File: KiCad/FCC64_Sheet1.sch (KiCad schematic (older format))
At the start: 23 parts, among them P1 JTAG, U1 27C256, U2 ATF1504AS, Y1 C64-Expansionport

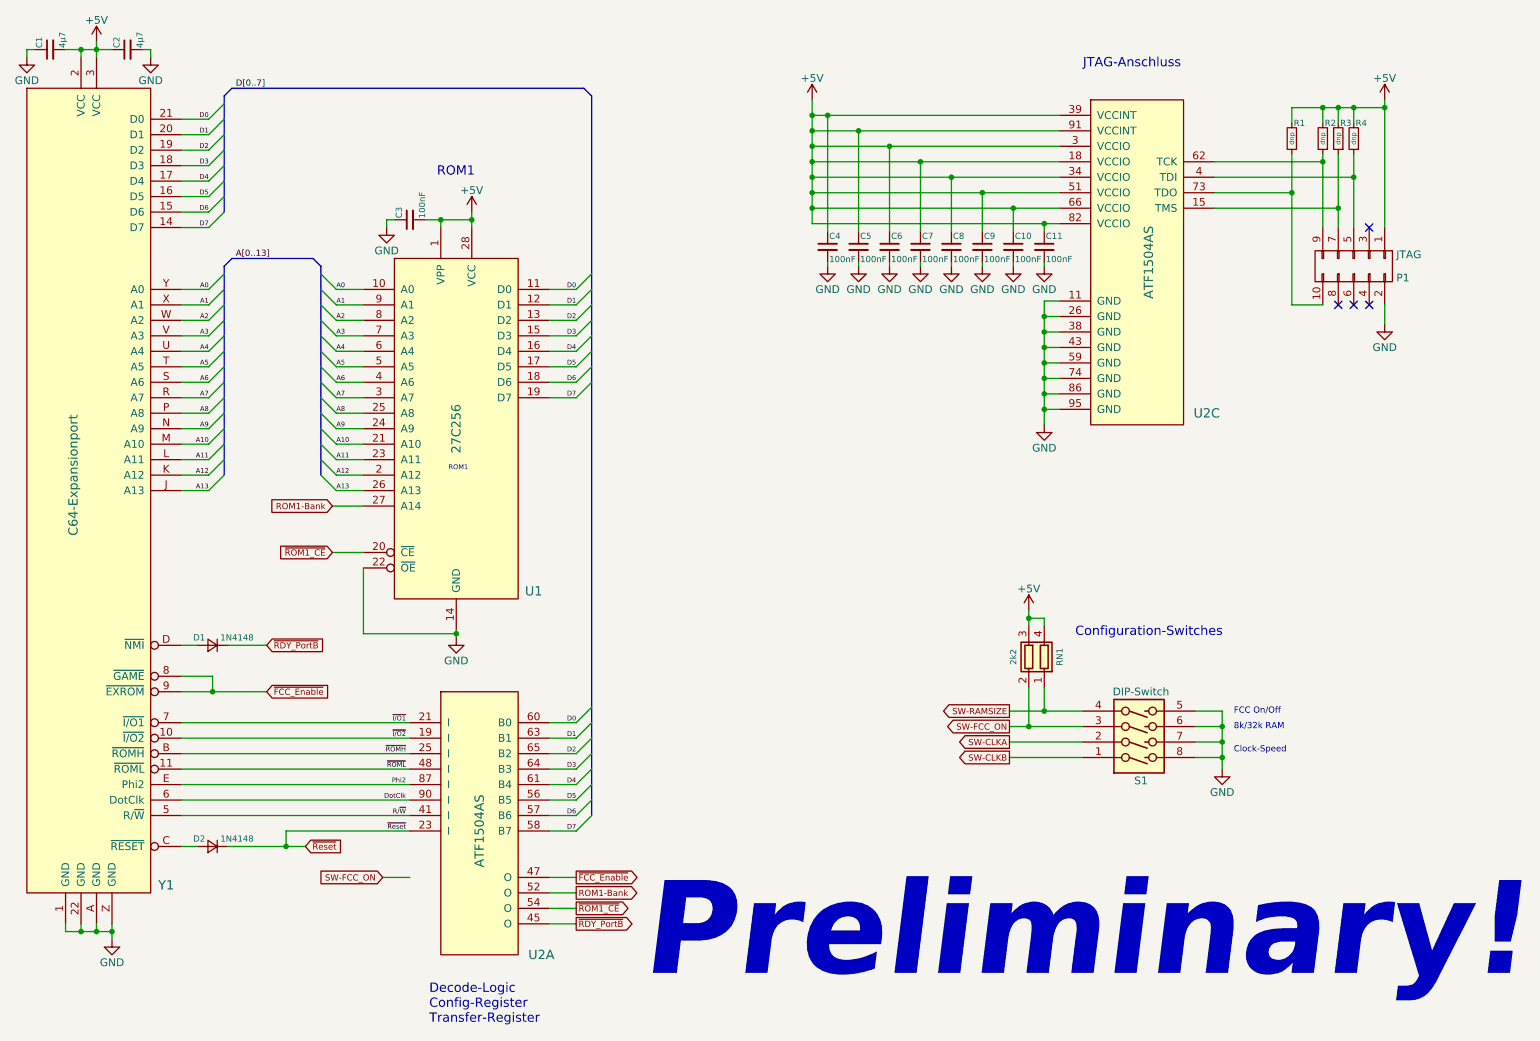
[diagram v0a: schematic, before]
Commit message: Various issues solved:
* QFP44-Footprint for W65C02 corrected
* FCC-On/Off deleted
* new battery supervisor ic TPS6513-01
* Battery Holder corrected
* Signals D5 and D7 to CPLD swapped
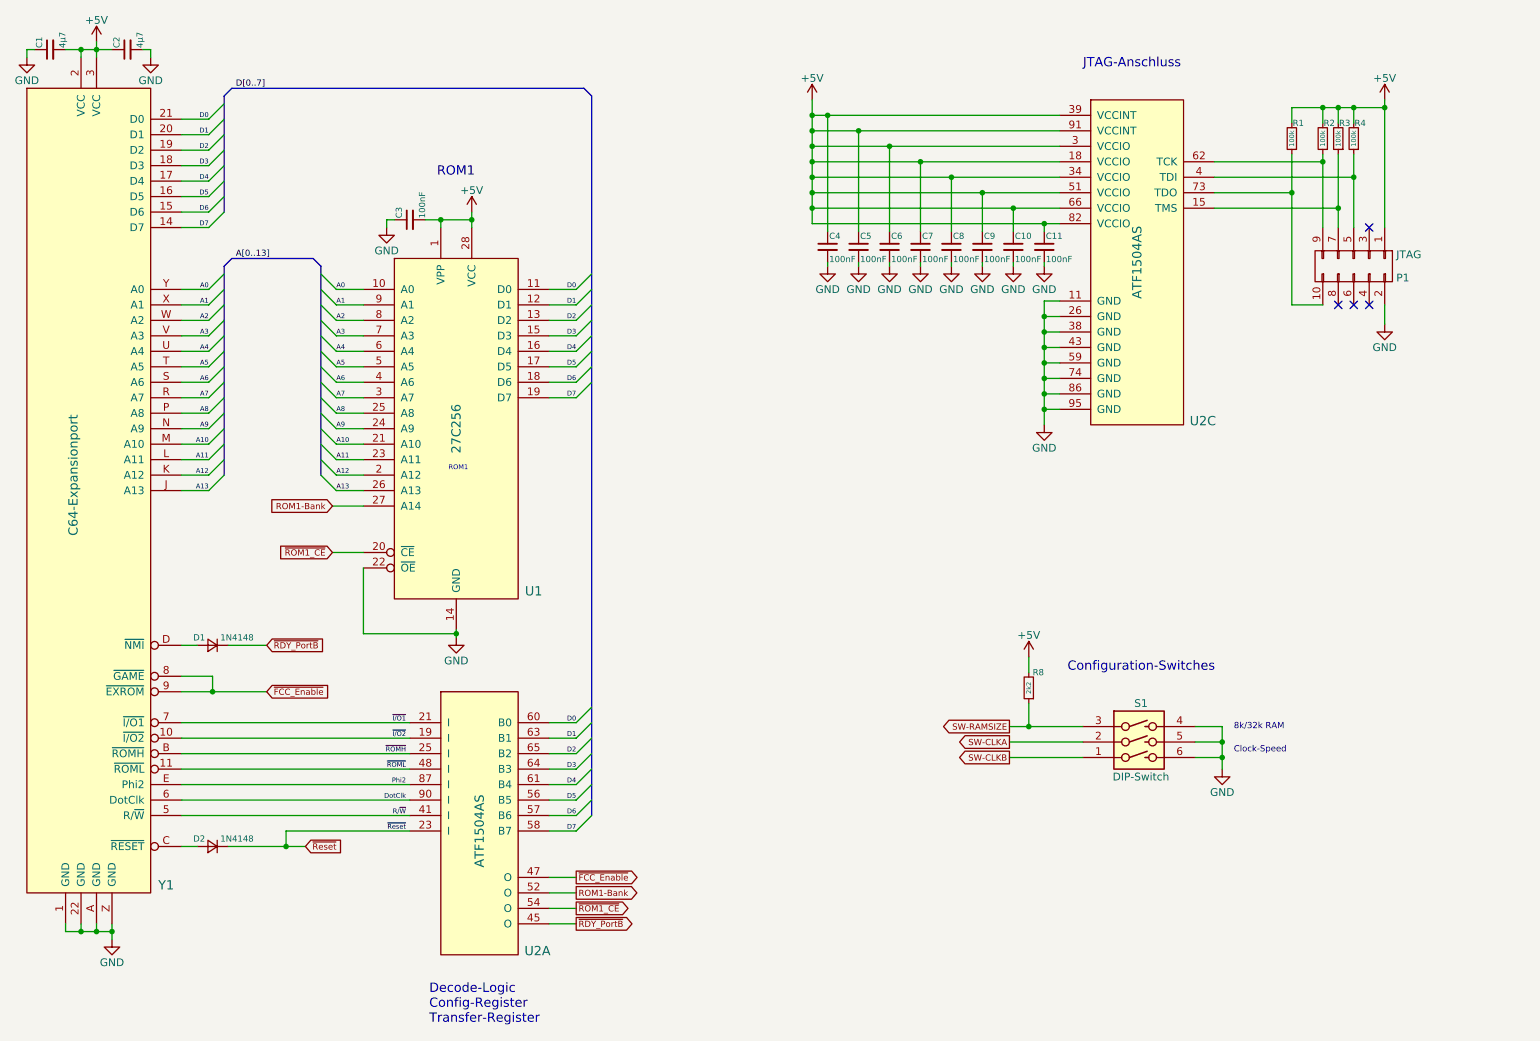
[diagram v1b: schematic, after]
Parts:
- removed RN1: 2k2, TTB_MyLib:TTB_RNet1206_2R, symbol R_Pack02
- removed S1: DIP-Switch, TTB_MyLib:TTB_DIPSwitch4, symbol DIP-Switch_4fach
- added R8: 2k2, TTB_MyLib:TTB_R0603, symbol R_Small
- added S1: DIP-Switch, TTB_MyLib:TTB_DIPSwitch3, symbol DIP-Switch_3fach
- R1, R2, R3, R4: value dnp -> 100k
- U2: footprint Housings_QFP:TQFP-100_14x14mm_Pitch0.5mm -> TTB_MyLib:TTB_TQFP100
- U2: footprint (none) -> TTB_MyLib:TTB_TQFP100
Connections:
- net +5V: now also R8.2
- net GND: now also S1.4 (P4), S1.5 (P5), S1.6 (P6)
- net SW-CLKA: now also S1.2 (P2)
- net SW-CLKB: now also S1.1 (P1)
- net SW-RAMSIZE: now also R8.1, S1.3 (P3)
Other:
- note removed: "FCC On/Off"
- note removed: "Preliminary!"
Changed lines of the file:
@@
 Sheet 2 3
 Title "The Final Chesscard (Forum64-Edition 2017)"
-Date "2017-05-04"
-Rev "-"
+Date "2017-07-09"
+Rev "1.0"
 Comp ""
 Comment1 ""
@@
 R/~W
 $Comp
-L ATF1504-RESCUE-FCC64 U?
-U 3 1 58FE4728
-P 8700 2475
-AR Path="/58FE4728" Ref="U?"  Part="3"
-AR Path="/58E6A155/58FE4728" Ref="U2"  Part="3"
-F 0 "U2" H 9150 1500 60  0000 C CNN
-F 1 "ATF1504AS" V 8775 2475 60  0000 C CNN
-F 2 "Housings_QFP:TQFP-100_14x14mm_Pitch0.5mm" H 8700 2275 60  0001 C CNN
-F 3 "" H 8700 2275 60  0000 C CNN
-	3    8700 2475
-	1    0    0    -1
-$EndComp
-$Comp
 L CONN_02X05 P1
 U 1 1 58FE4D90
@@
 U 1 1 58FE6795
 P 9900 1675
-F 0 "R2" H 9815 1575 40  0000 L CNN
-F 1 "dnp" V 9900 1675 31  0000 C CNN
+F 0 "R2" H 9895 1575 40  0000 R CNN
+F 1 "100k" V 9900 1675 31  0000 C CNN
 F 2 "TTB_MyLib:TTB_R0603" H 9900 1675 50  0001 C CNN
 F 3 "" H 9900 1675 50  0000 C CNN
@@
 U 1 1 58FE69EA
 P 10000 1675
-F 0 "R3" H 9915 1575 40  0000 L CNN
-F 1 "dnp" V 10000 1675 31  0000 C CNN
+F 0 "R3" H 9995 1575 40  0000 R CNN
+F 1 "100k" V 10000 1675 31  0000 C CNN
 F 2 "TTB_MyLib:TTB_R0603" H 10000 1675 50  0001 C CNN
 F 3 "" H 10000 1675 50  0000 C CNN
@@
 U 1 1 58FE6A19
 P 10100 1675
-F 0 "R4" H 10015 1575 40  0000 L CNN
-F 1 "dnp" V 10100 1675 31  0000 C CNN
+F 0 "R4" H 10095 1575 40  0000 R CNN
+F 1 "100k" V 10100 1675 31  0000 C CNN
 F 2 "TTB_MyLib:TTB_R0603" H 10100 1675 50  0001 C CNN
 F 3 "" H 10100 1675 50  0000 C CNN
@@
 U 1 1 58FE6F40
 P 9700 1675
-F 0 "R1" H 9615 1575 40  0000 L CNN
-F 1 "dnp" V 9700 1675 31  0000 C CNN
+F 0 "R1" H 9695 1575 40  0000 R CNN
+F 1 "100k" V 9700 1675 31  0000 C CNN
 F 2 "TTB_MyLib:TTB_R0603" H 9700 1675 50  0001 C CNN
 F 3 "" H 9700 1675 50  0000 C CNN
@@
 	1525 1100 1525 1150
 Connection ~ 1875 1100
-Text GLabel 3825 6450 0    40   Input ~ 0
-SW-FCC_ON
-Wire Wire Line
-	3825 6450 4000 6450
-Text Notes 8300 4900 0    60   ~ 0
+Text Notes 8250 5125 0    60   ~ 0
 Configuration-Switches
-Text GLabel 7875 5375 0    40   Output ~ 0
+Text GLabel 7875 5475 0    40   Output ~ 0
 SW-RAMSIZE
 Text GLabel 7875 5675 0    40   Output ~ 0
@@
 L +5V #PWR020
 U 1 1 590A9614
-P 8000 4725
-F 0 "#PWR020" H 8000 4575 50  0001 C CNN
-F 1 "+5V" H 8000 4865 50  0000 C CNN
-F 2 "" H 8000 4725 50  0000 C CNN
-F 3 "" H 8000 4725 50  0000 C CNN
-	1    8000 4725
-	1    0    0    -1
-$EndComp
-Wire Wire Line
-	7875 5375 8350 5375
+P 8000 5025
+F 0 "#PWR020" H 8000 4875 50  0001 C CNN
+F 1 "+5V" H 8000 5165 50  0000 C CNN
+F 2 "" H 8000 5025 50  0000 C CNN
+F 3 "" H 8000 5025 50  0000 C CNN
+	1    8000 5025
+	1    0    0    -1
+$EndComp
 Wire Wire Line
 	7875 5475 8350 5475
 Wire Wire Line
 	7875 5575 8350 5575
-Text GLabel 7875 5475 0    40   Output ~ 0
-SW-FCC_ON
 $Comp
 L GND #PWR021
@@
 	9250 5575 9075 5575
 Wire Wire Line
-	9250 5375 9250 5750
-Wire Wire Line
 	9075 5475 9250 5475
 Connection ~ 9250 5575
 Wire Wire Line
-	9075 5375 9250 5375
-Connection ~ 9250 5475
-$Comp
-L DIP-Switch_4fach S1
-U 1 1 590A9635
-P 8725 5525
-F 0 "S1" H 8725 5825 50  0000 C CNN
-F 1 "DIP-Switch" H 8725 5250 50  0000 C CNN
-F 2 "TTB_MyLib:TTB_DIPSwitch4" H 8700 5525 50  0001 C CNN
-F 3 "" H 8700 5525 50  0000 C CNN
-	1    8725 5525
-	1    0    0    1
-$EndComp
-Wire Wire Line
-	9075 5675 9250 5675
+	9250 5675 9075 5675
 Connection ~ 9250 5675
 Text Notes 9325 5500 0    40   ~ 0
 8k/32k RAM
-Text Notes 9325 5400 0    40   ~ 0
-FCC On/Off
 Text Notes 9325 5650 0    40   ~ 0
 Clock-Speed
-$Comp
-L R_Pack02 RN1
-U 1 1 590C2924
-P 8000 5025
-F 0 "RN1" V 7800 5025 40  0000 C CNN
-F 1 "2k2" V 8100 5025 40  0000 C CNN
-F 2 "TTB_MyLib:TTB_RNet1206_2R" V 8175 5025 50  0001 C CNN
-F 3 "" H 8000 5025 50  0000 C CNN
-	1    8000 5025
-	-1   0    0    -1
-$EndComp
 Wire Wire Line
 	7875 5675 8350 5675
 Wire Wire Line
-	8000 4825 8000 4725
-Wire Wire Line
-	8100 4825 8100 4775
-Wire Wire Line
-	8100 4775 8000 4775
-Connection ~ 8000 4775
-Text Notes 11225 7150 2    600  Italic 120
-Preliminary!
+	8000 5125 8000 5025
+Wire Wire Line
+	8000 5325 8000 5475
+Connection ~ 8000 5475
+$Comp
+L ATF1504-RESCUE-FCC64 U2
+U 3 1 595BDF95
+P 8700 2475
+AR Path="/595BDF95" Ref="U2"  Part="3"
+AR Path="/58E6A155/595BDF95" Ref="U2"  Part="3"
+F 0 "U2" H 9125 1450 60  0000 C CNN
+F 1 "ATF1504AS" V 8700 2475 60  0000 C CNN
+F 2 "TTB_MyLib:TTB_TQFP100" H 8700 2275 60  0001 C CNN
+F 3 "" H 8700 2275 60  0000 C CNN
+	3    8700 2475
+	1    0    0    -1
+$EndComp
+$Comp
+L DIP-Switch_3fach S1
+U 1 1 59624767
+P 8725 5575
+F 0 "S1" H 8725 5825 50  0000 C CNN
+F 1 "DIP-Switch" H 8725 5350 50  0000 C CNN
+F 2 "TTB_MyLib:TTB_DIPSwitch3" H 8700 5575 50  0001 C CNN
+F 3 "" H 8700 5575 50  0000 C CNN
+	1    8725 5575
+	1    0    0    -1
+$EndComp
+Wire Wire Line
+	9250 5475 9250 5750
+$Comp
+L R_Small R8
+U 1 1 59626FD6
+P 8000 5225
+F 0 "R8" H 7975 5125 40  0000 R CNN
+F 1 "2k2" V 8000 5225 31  0000 C CNN
+F 2 "TTB_MyLib:TTB_R0603" H 8000 5225 50  0001 C CNN
+F 3 "" H 8000 5225 50  0000 C CNN
+	1    8000 5225
+	-1   0    0    1
+$EndComp
 $Comp
 L ATF1504 U2
-U 1 1 59219D32
+U 1 1 59631F49
 P 4450 6150
-F 0 "U2" H 4850 5350 60  0000 C CNN
+F 0 "U2" H 4825 5375 60  0000 C CNN
 F 1 "ATF1504AS" V 4450 6150 60  0000 C CNN
-F 2 "" H 4450 5950 60  0000 C CNN
+F 2 "TTB_MyLib:TTB_TQFP100" H 4450 5950 60  0001 C CNN
 F 3 "" H 4450 5950 60  0000 C CNN
 	1    4450 6150
 	1    0    0    -1
 $EndComp
-Wire Wire Line
-	8000 5225 8000 5475
-Connection ~ 8000 5475
-Wire Wire Line
-	8100 5225 8100 5375
-Connection ~ 8100 5375
 $EndSCHEMATC

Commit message: Tidying up for initial batch
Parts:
- C1, C2: value 4µ7 -> 10µ
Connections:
- net GND: now also S1.1 (P1), S1.2 (P2), S1.3 (P3); no longer S1.4 (P4), S1.5 (P5), S1.6 (P6)
- net SW-CLKA: now also S1.5 (P5); no longer S1.2 (P2)
- net SW-CLKB: now also S1.4 (P4); no longer S1.1 (P1)
- net SW-RAMSIZE: now also S1.6 (P6); no longer S1.3 (P3)
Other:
- note added: "Power Supply & JTAG-Port"
- note removed: "JTAG-Anschluss"
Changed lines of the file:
@@
 Wire Wire Line
 	5075 6450 4900 6450
-Text Notes 8350 1225 0    60   ~ 0
-JTAG-Anschluss
+Text Notes 8075 1225 0    60   ~ 0
+Power Supply & JTAG-Port
 Text Label 3975 5450 2    31   ~ 0
 ~I/O1
@@
 P 2175 1100
 F 0 "C2" H 2185 1170 40  0000 L CNN
-F 1 "4µ7" H 2185 1020 40  0000 L CNN
+F 1 "10µ" H 2185 1020 40  0000 L CNN
 F 2 "TTB_MyLib:TTB_C1206" H 2175 1100 50  0001 C CNN
 F 3 "" H 2175 1100 50  0000 C CNN
@@
 P 1675 1100
 F 0 "C1" H 1685 1170 40  0000 L CNN
-F 1 "4µ7" H 1685 1020 40  0000 L CNN
+F 1 "10µ" H 1685 1020 40  0000 L CNN
 F 2 "TTB_MyLib:TTB_C1206" H 1675 1100 50  0001 C CNN
 F 3 "" H 1675 1100 50  0000 C CNN
@@
 Text Notes 8250 5125 0    60   ~ 0
 Configuration-Switches
+Text GLabel 7875 5675 0    40   Output ~ 0
+SW-RAMSIZE
 Text GLabel 7875 5475 0    40   Output ~ 0
-SW-RAMSIZE
-Text GLabel 7875 5675 0    40   Output ~ 0
 SW-CLKB
 Text GLabel 7875 5575 0    40   Output ~ 0
@@
 $EndComp
 Wire Wire Line
-	7875 5475 8350 5475
-Wire Wire Line
 	7875 5575 8350 5575
 $Comp
@@
 	9250 5675 9075 5675
 Connection ~ 9250 5675
-Text Notes 9325 5500 0    40   ~ 0
+Text Notes 9325 5700 0    40   ~ 0
 8k/32k RAM
-Text Notes 9325 5650 0    40   ~ 0
+Text Notes 9325 5550 0    40   ~ 0
 Clock-Speed
 Wire Wire Line
@@
 Wire Wire Line
 	8000 5125 8000 5025
-Wire Wire Line
-	8000 5325 8000 5475
-Connection ~ 8000 5475
 $Comp
 L ATF1504-RESCUE-FCC64 U2
@@
 L DIP-Switch_3fach S1
 U 1 1 59624767
-P 8725 5575
-F 0 "S1" H 8725 5825 50  0000 C CNN
-F 1 "DIP-Switch" H 8725 5350 50  0000 C CNN
-F 2 "TTB_MyLib:TTB_DIPSwitch3" H 8700 5575 50  0001 C CNN
-F 3 "" H 8700 5575 50  0000 C CNN
-	1    8725 5575
-	1    0    0    -1
+P 8700 5575
+F 0 "S1" H 8700 5825 50  0000 C CNN
+F 1 "DIP-Switch" H 8700 5350 50  0000 C CNN
+F 2 "TTB_MyLib:TTB_DIPSwitch3" H 8675 5575 50  0001 C CNN
+F 3 "" H 8675 5575 50  0000 C CNN
+	1    8700 5575
+	-1   0    0    -1
 $EndComp
 Wire Wire Line
@@
 	1    0    0    -1
 $EndComp
+Wire Wire Line
+	7875 5475 8350 5475
+Wire Wire Line
+	8000 5325 8000 5675
+Connection ~ 8000 5675
 $EndSCHEMATC
